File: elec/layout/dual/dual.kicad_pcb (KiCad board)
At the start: 2 copper layers, 9 parts, among them U1 ?

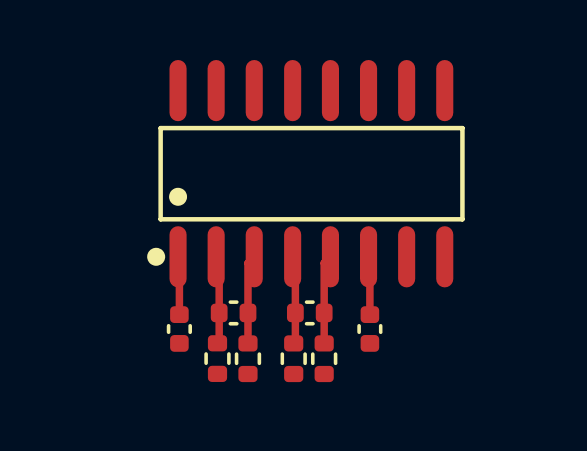
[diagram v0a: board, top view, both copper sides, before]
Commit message: relink with 0.3 compiler
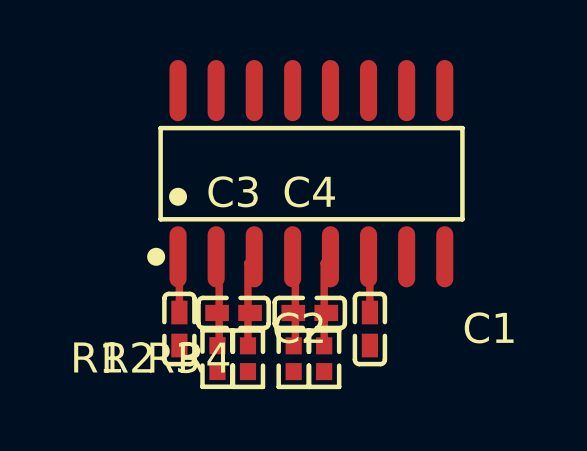
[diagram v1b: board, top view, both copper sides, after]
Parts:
- C1, C2, C3, C4: value 16V 100nF X7R ±10% 0402 Multilayer Ceramic Capacitors MLCC - SMD/SMT ROHS -> 100nF ±10% 16V X7R; footprint lib:C0402 -> atopile:C0402-b3ef17
- R1, R2, R3, R4: value 62.5mW Thick Film Resistors 50V ±100ppm/℃ ±1% 49.9Ω 0402 Chip Resistor - Surface Mount ROHS -> 51Ω ±1% 62.5mW; footprint lib:R0402 -> atopile:R0402-56259e
- U1: value ? -> (none)
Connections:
- net avdd_ldo renamed AVDD_LDO
- net drdy renamed DRDY
- net refp renamed REFP
- net sda renamed SDA
- net vbg renamed VBG
- net vcc renamed DVDD
- net vin1n renamed VIN1N
- net vin1p renamed VIN1P
- net vin2n renamed VIN2N
- net vin2p renamed VIN2P
- net xin renamed XIN
- net xout renamed XOUT
- R1 pad 1: n -> n-1
- R2 pad 1: p -> p-1
- R3 pad 1: n-1 -> n
- R4 pad 1: p-1 -> p
